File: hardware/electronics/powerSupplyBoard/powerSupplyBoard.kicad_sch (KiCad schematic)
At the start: 27 parts, among them J1 USB_C_Receptacle_USB2.0, J3 615004143821, J4 PRPC009SBAN-M71RC, SW1 PTS647, SW2 SS-12D07, U1 STM32L052K6, U2 AP2112K-3.3, U3 SN65HVD230QDR, Y1 ECS-327ATQMV

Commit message: fixed properties for Tag-Connect and push button
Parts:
- J2: DKPN (none) -> N/A; MPN (none) -> N/A; Manufacturer (none) -> N/A
- SW1: DKPN (none) -> PTS647SK38SMTR2LFSCT-ND; MPN (none) -> PTS 647 SK38 SMTR2 LFS; Manufacturer (none) -> C&K
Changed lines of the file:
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@@
 			)
 		)
-		(property "Datasheet" "~"
+		(property "Datasheet" "datasheets/CK-Switches-PTS647.pdf"
 			(at 196.85 110.49 0)
 			(effects
@@
 			)
 		)
-		(property "Manufacturer" "~"
+		(property "Manufacturer" "C&K"
 			(at 196.85 111.125 0)
 			(do_not_autoplace yes)
@@
 			)
 		)
-		(property "MPN" "~"
+		(property "MPN" "PTS 647 SK38 SMTR2 LFS"
 			(at 196.85 110.49 0)
 			(effects
@@
 			)
 		)
-		(property "DKPN" "~"
+		(property "DKPN" "PTS647SK38SMTR2LFSCT-ND"
 			(at 196.85 110.49 0)
 			(effects
@@
 			)
 		)
-		(property "Description" ""
+		(property "Description" "Tag-Connect TC2050-FP board connector"
 			(at 87.63 135.89 0)
 			(effects
@@
 			)
 		)
-		(property "Manufacturer" "~"
+		(property "Manufacturer" "N/A"
 			(at 87.63 135.89 0)
 			(effects
@@
 			)
 		)
-		(property "MPN" "~"
+		(property "MPN" "N/A"
 			(at 87.63 135.89 0)
 			(effects
@@
 			)
 		)
-		(property "DKPN" "~"
+		(property "DKPN" "N/A"
 			(at 87.63 135.89 0)
 			(effects

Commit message: redefined footprint paths
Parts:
- C1, C2: footprint DS-Capacitors-SMD:MLCC0805 -> lib_fp:MLCC0805
- C10, C11, C5: footprint DS-Capacitors-SMD:MLCC0603 -> lib_fp:MLCC0603; MPN 06035C104K4T4A -> KAM15AR71H104KM
- C3: footprint DS-Capacitors-SMD:MLCC0603 -> lib_fp:MLCC0603; MPN 0805ZC475MAT2A -> KGM21AR71A475MU
- C4, C7, C8, C9: footprint DS-Capacitors-SMD:MLCC0603 -> lib_fp:MLCC0603
- C6: footprint DS-Capacitors-SMD:MLCC0805 -> lib_fp:MLCC0603
- J1: footprint DS-Connector-USB:MOLEX_2171790001 -> lib_fp:MOLEX_2171790001
- J2: footprint DS-Connectors-SMD:TC2050-FP -> lib_fp:TC2050-FP
- J3: footprint DS-Connectors-Network:615004143821 -> lib_fp:615004143821
- J4: footprint DS-Rectangular-Connectors:conn_01x09_254_right_angle -> lib_fp:conn_01x09_254_right_angle
- R1, R2, R3, R4, R5, R6: footprint DS-Resistors-SMD:CRCW0603 -> lib_fp:CRCW0603
- SW1: footprint DS-Switches:SW_4.5x4.5 -> lib_fp:SW_4.5x4.5
- SW2: footprint DS-Switches:SS-12D07-VG_GA_PA -> lib_fp:SS-12D07-VG_GA_PA
- U1: footprint DS-Microcontrollers:UFQFPN32 -> lib_fp:UFQFPN32
- U2: footprint DS-Package-SO:SOT23-5P95_280X300X110L40X38N -> lib_fp:SOT23-5P95_280X300X110L40X38N
- U3: footprint DS-Package-SO:SOIC8P127_490X600X195L83X42N -> lib_fp:SOIC8P127_490X600X195L83X42N
- Y1: footprint DS-Crystals:EXC-34Q -> lib_fp:EXC-34Q
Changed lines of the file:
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@@
 			)
 		)
-		(property "Footprint" "DS-Capacitors-SMD:MLCC0603"
+		(property "Footprint" "lib_fp:MLCC0603"
 			(at 114.3 51.435 0)
 			(effects
@@
 			)
 		)
-		(property "MPN" "06035C104K4T4A"
+		(property "MPN" "KAM15AR71H104KM"
 			(at 114.3 51.435 0)
 			(effects
@@
 			)
 		)
-		(property "Footprint" "DS-Switches:SW_4.5x4.5"
+		(property "Footprint" "lib_fp:SW_4.5x4.5"
 			(at 207.645 110.49 0)
 			(effects
@@
 			)
 		)
-		(property "Footprint" "DS-Capacitors-SMD:MLCC0603"
+		(property "Footprint" "lib_fp:MLCC0603"
 			(at 99.06 51.435 0)
 			(effects
@@
 			)
 		)
-		(property "MPN" "0805ZC475MAT2A"
+		(property "MPN" "KGM21AR71A475MU"
 			(at 99.06 51.435 0)
 			(effects
@@
 			)
 		)
-		(property "Footprint" "DS-Connector-USB:MOLEX_2171790001"
+		(property "Footprint" "lib_fp:MOLEX_2171790001"
 			(at 25.4 38.1 0)
 			(effects
@@
 			)
 		)
-		(property "Footprint" "DS-Microcontrollers:UFQFPN32"
+		(property "Footprint" "lib_fp:UFQFPN32"
 			(at 104.14 88.9 0)
 			(effects
@@
 			)
 		)
-		(property "Footprint" "DS-Package-SO:SOT23-5P95_280X300X110L40X38N"
+		(property "Footprint" "lib_fp:SOT23-5P95_280X300X110L40X38N"
 			(at 72.39 19.05 0)
 			(effects
@@
 			)
 		)
-		(property "Footprint" "DS-Capacitors-SMD:MLCC0603"
+		(property "Footprint" "lib_fp:MLCC0603"
 			(at 184.15 109.855 0)
 			(effects
@@
 			)
 		)
-		(property "Footprint" "DS-Resistors-SMD:CRCW0603"
+		(property "Footprint" "lib_fp:CRCW0603"
 			(at 38.1 24.13 0)
 			(effects
@@
 			)
 		)
-		(property "Footprint" "DS-Switches:SS-12D07-VG_GA_PA"
+		(property "Footprint" "lib_fp:SS-12D07-VG_GA_PA"
 			(at 177.8 127 0)
 			(effects
@@
 			)
 		)
-		(property "Footprint" "DS-Package-SO:SOIC8P127_490X600X195L83X42N"
+		(property "Footprint" "lib_fp:SOIC8P127_490X600X195L83X42N"
 			(at 78.74 76.2 0)
 			(effects
@@
 			)
 		)
-		(property "Footprint" "DS-Capacitors-SMD:MLCC0805"
+		(property "Footprint" "lib_fp:MLCC0603"
 			(at 172.72 51.435 0)
 			(effects
@@
 			)
 		)
-		(property "Footprint" "DS-Resistors-SMD:CRCW0603"
+		(property "Footprint" "lib_fp:CRCW0603"
 			(at 177.8 80.01 0)
 			(effects
@@
 			)
 		)
-		(property "Footprint" "DS-Resistors-SMD:CRCW0603"
+		(property "Footprint" "lib_fp:CRCW0603"
 			(at 166.37 127 90)
 			(effects
@@
 			)
 		)
-		(property "Footprint" "DS-Capacitors-SMD:MLCC0805"
+		(property "Footprint" "lib_fp:MLCC0805"
 			(at 82.55 24.765 0)
 			(effects
@@
 			)
 		)
-		(property "Footprint" "DS-Capacitors-SMD:MLCC0603"
+		(property "Footprint" "lib_fp:MLCC0603"
 			(at 179.07 104.775 0)
 			(effects
@@
 			)
 		)
-		(property "Footprint" "DS-Capacitors-SMD:MLCC0603"
+		(property "Footprint" "lib_fp:MLCC0603"
 			(at 88.9 62.865 0)
 			(effects
@@
 			)
 		)
-		(property "MPN" "06035C104K4T4A"
+		(property "MPN" "KAM15AR71H104KM"
 			(at 88.9 62.865 0)
 			(effects
@@
 			)
 		)
-		(property "Footprint" "DS-Resistors-SMD:CRCW0603"
+		(property "Footprint" "lib_fp:CRCW0603"
 			(at 185.42 80.01 0)
 			(effects
@@
 			)
 		)
-		(property "Footprint" "DS-Capacitors-SMD:MLCC0603"
+		(property "Footprint" "lib_fp:MLCC0603"
 			(at 180.34 51.435 0)
 			(effects
@@
 			)
 		)
-		(property "Footprint" "DS-Rectangular-Connectors:conn_01x09_254_right_angle"
+		(property "Footprint" "lib_fp:conn_01x09_254_right_angle"
 			(at 22.86 172.72 0)
 			(effects
@@
 			)
 		)
-		(property "Footprint" "DS-Capacitors-SMD:MLCC0805"
+		(property "Footprint" "lib_fp:MLCC0805"
 			(at 55.88 24.765 0)
 			(effects
@@
 			)
 		)
-		(property "Footprint" "DS-Capacitors-SMD:MLCC0603"
+		(property "Footprint" "lib_fp:MLCC0603"
 			(at 196.85 121.285 0)
 			(effects
@@
 			)
 		)
-		(property "MPN" "06035C104K4T4A"
+		(property "MPN" "KAM15AR71H104KM"
 			(at 196.85 121.285 0)
 			(effects
@@
 			)
 		)
-		(property "Footprint" "DS-Resistors-SMD:CRCW0603"
+		(property "Footprint" "lib_fp:CRCW0603"
 			(at 46.99 24.13 0)
 			(effects
@@
 			)
 		)
-		(property "Footprint" "DS-Resistors-SMD:CRCW0603"
+		(property "Footprint" "lib_fp:CRCW0603"
 			(at 68.58 73.66 0)
 			(effects
@@
 			)
 		)
-		(property "Footprint" "DS-Connectors-Network:615004143821"
+		(property "Footprint" "lib_fp:615004143821"
 			(at 50.8 73.66 0)
 			(effects
@@
 			)
 		)
-		(property "Footprint" "DS-Connectors-SMD:TC2050-FP"
+		(property "Footprint" "lib_fp:TC2050-FP"
 			(at 87.63 135.89 0)
 			(effects
@@
 			)
 		)
-		(property "Footprint" "DS-Crystals:EXC-34Q"
+		(property "Footprint" "lib_fp:EXC-34Q"
 			(at 165.1 101.6 90)
 			(effects
@@
 			)
 		)
-		(property "Footprint" "DS-Capacitors-SMD:MLCC0603"
+		(property "Footprint" "lib_fp:MLCC0603"
 			(at 106.68 51.435 0)
 			(effects

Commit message: updated component references and sizes
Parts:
- removed C11: 100nF, lib_fp:MLCC0603, symbol lib_sch:C_2
- removed J3: 615004143821, lib_fp:615004143821, symbol lib_sch:RJ11
- removed R6: 120R, lib_fp:CRCW0603, symbol lib_sch:R
- removed U3: SN65HVD230QDR, lib_fp:SOIC8P127_490X600X195L83X42N, symbol lib_sch:SN65HVD23xQ
- C1, C2: DKPN 478-KGM21AR71C106KUCT-ND -> 478-KAM21AR71A106MUCT-ND; MPN KGM21AR71C106KU -> KAM21AR71A106MU; Tolerance 10% -> 20%; Voltage Rating 16V -> 10V
- C3: DKPN 478-KGM21AR71A475MUCT-ND -> 478-KAM15CR70J475KTCT-ND; MPN KGM21AR71A475MU -> KAM15CR70J475KT; Package 0805 -> 0603; Tolerance 20% -> 10%; Voltage Rating 10V -> 6V3
- C6: DKPN 478-KGM21AR71H105KLCT-ND -> 478-KAM15AR71C105KTCT-ND; MPN 08055C105KAT4A -> KAM15AR71C105KT; Package 0805 -> 0603; Voltage Rating 50V -> 16V
- C7: footprint lib_fp:MLCC0603 -> lib_fp:MLCC0402; DKPN 478-KGM15AR71C103KTCT-ND -> 478-KAM05AR71H103KHCT-ND; MPN KGM15AR71C103KT -> KAM05AR71H103KH; Package 0603 -> 0402; Voltage Rating 16V -> 50V
- R1, R2: footprint lib_fp:CRCW0603 -> lib_fp:CRCW0402; DKPN 541-5.1KGCT-ND -> 541-5.10KLCT-ND; MPN CRCW06035K10JNEA -> CRCW04025K10FKED; Package 0603 -> 0402; Power Rating 100mW -> 62.5mW; Tolerance 5% -> 1%
- R3, R4, R5: footprint lib_fp:CRCW0603 -> lib_fp:CRCW0402; DKPN 541-10KGCT-ND -> 541-10KJCT-ND; MPN CRCW060310K0JNEA -> CRCW040210K0JNED; Package 0603 -> 0402; Power Rating 100mW -> 62.5mW
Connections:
- net CAN_MODE: no longer names the net of U1.10 (PA4)
- net CAN_RXD: no longer names the net of U1.9 (PA3)
- net CAN_TXD: no longer names the net of U1.8 (PA2)
- no-connect marks 14 -> 15
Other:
- note removed: "+3V3 CANbus Transceiver"
- note removed: "RJ11 Jack"
- moved on the sheet: J4

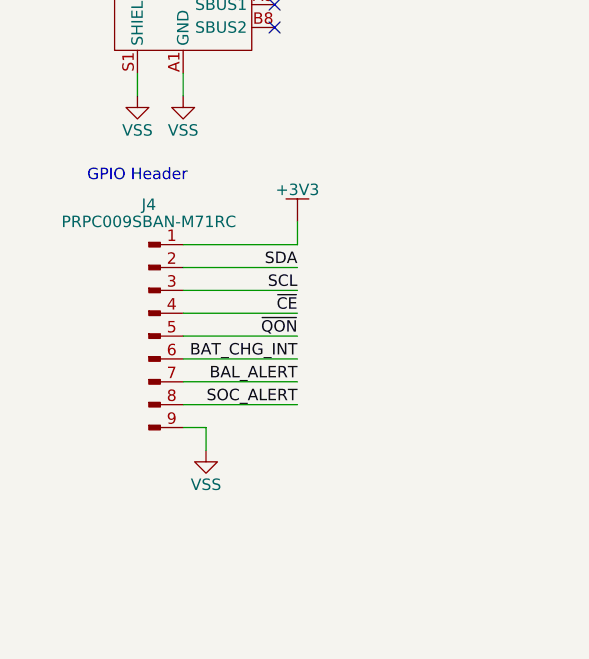
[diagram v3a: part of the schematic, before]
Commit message: removed gpio header
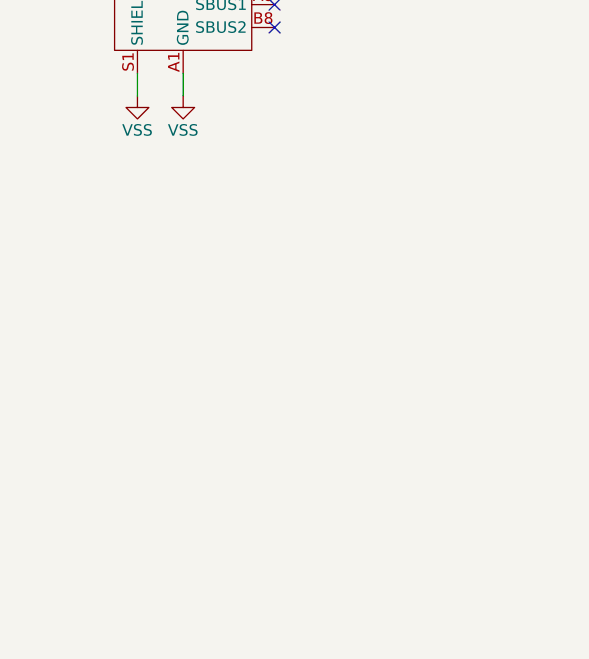
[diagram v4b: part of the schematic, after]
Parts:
- removed J4: PRPC009SBAN-M71RC, lib_fp:conn_01x09_254_right_angle, symbol lib_sch:Conn_01x09_Pin
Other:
- note removed: "GPIO Header"

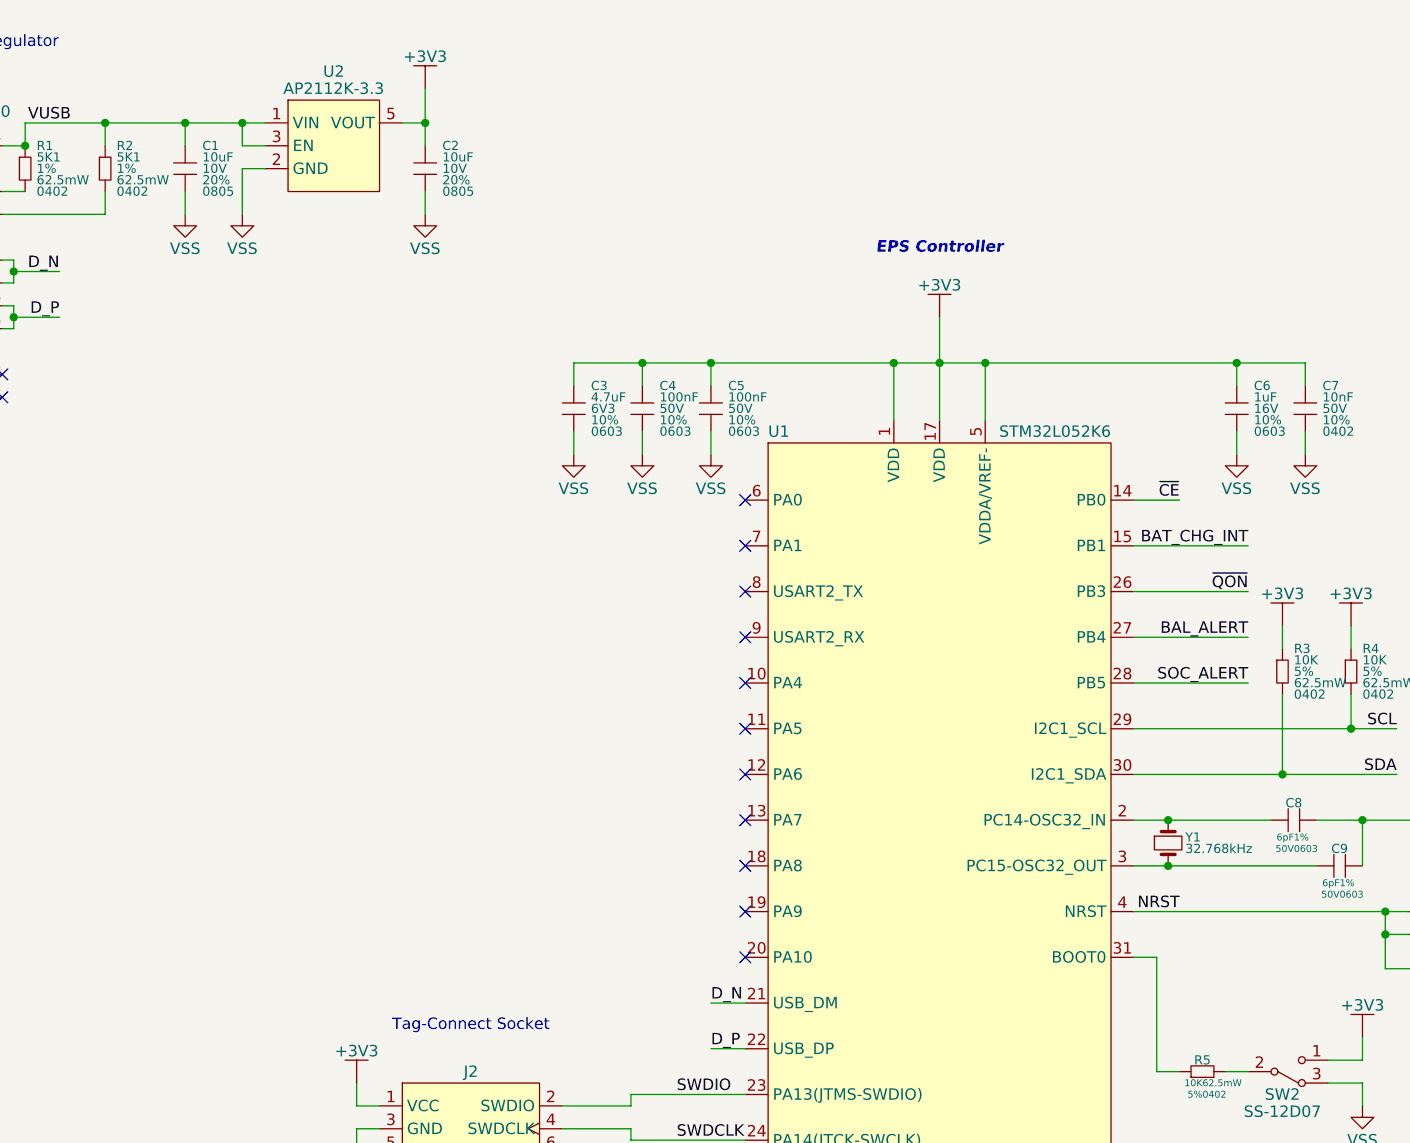
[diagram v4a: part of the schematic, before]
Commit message: added LEDs and remapped some pins for easier routing
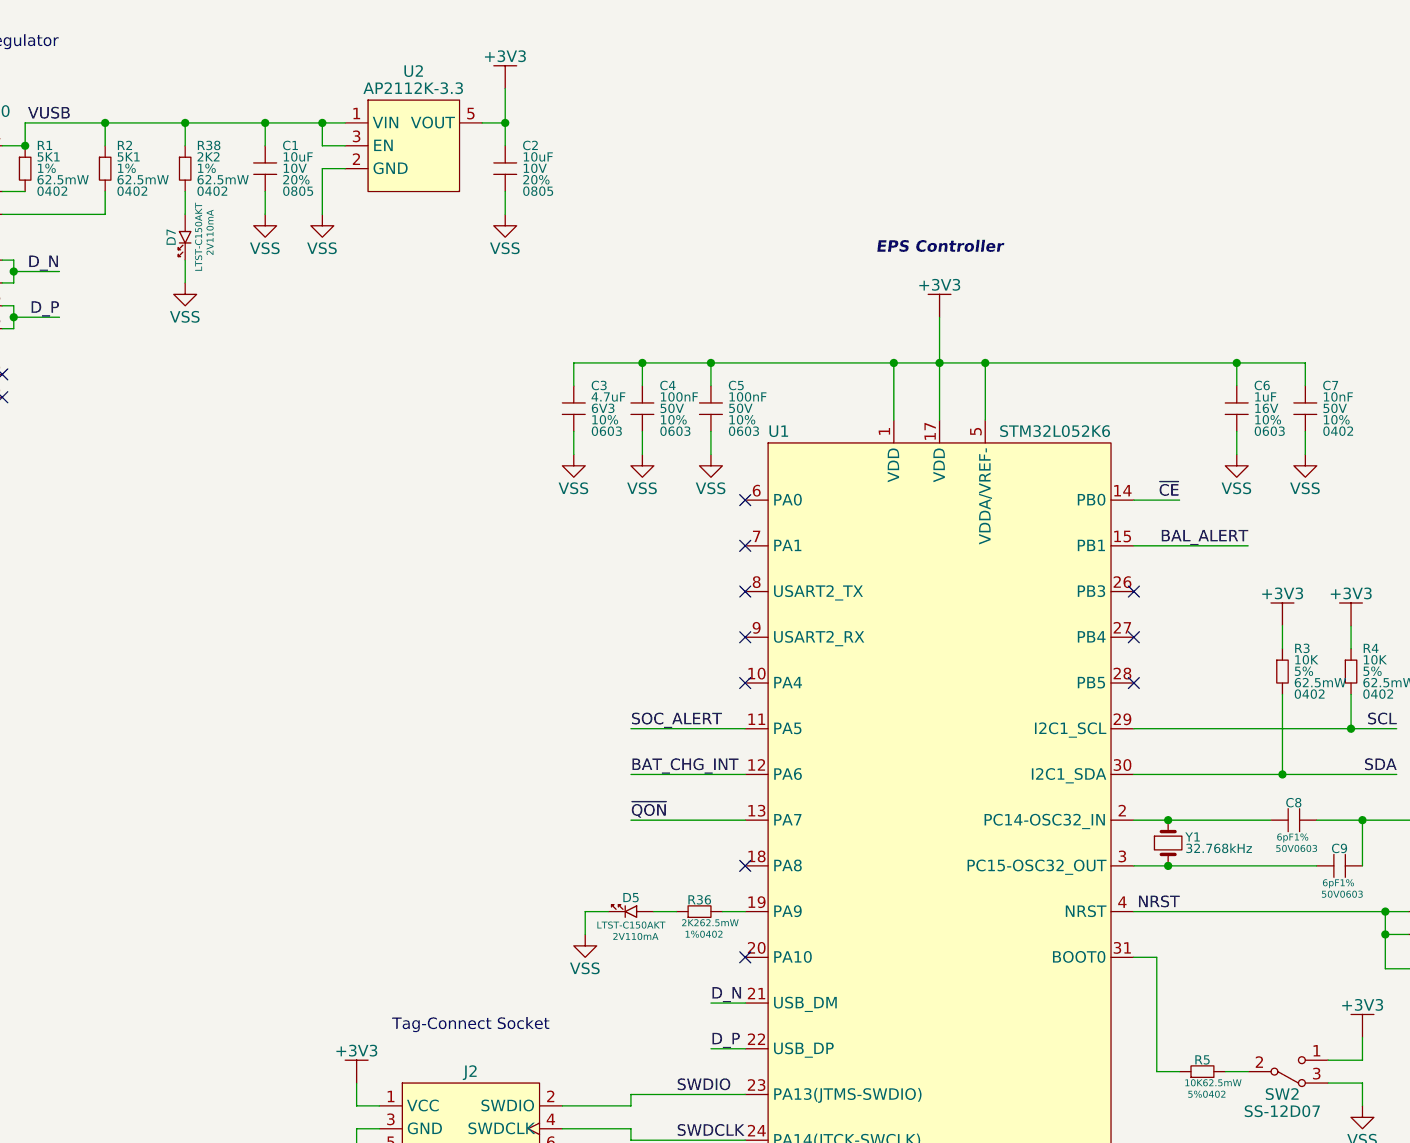
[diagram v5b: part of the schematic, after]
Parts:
- added D5, D7: LTST-C150AKT, lib_fp:LTST-1206, symbol lib_sch:LED_horizontal
- added R36: 2K2, lib_fp:CRCW0402, symbol lib_sch:R_horizontal
- added R38: 2K2, lib_fp:CRCW0402, symbol lib_sch:R
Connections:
- net BAL_ALERT: now also U1.15 (PB1); no longer U1.27 (PB4)
- net BAT_CHG_INT: now also U1.12 (PA6); no longer U1.15 (PB1)
- net SOC_ALERT: now also U1.11 (PA5); no longer U1.28 (PB5)
- net VSS: now also D5.2, D7.2
- net VUSB: now also R38.1
- net ~{QON}: now also U1.13 (PA7); no longer U1.26 (PB3)
- net at U1.19 (PA9): now also R36.2
- new net: D7.1, R38.2
- new net: D5.1, R36.1
- no-connect marks 15 -> 14
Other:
- moved on the sheet: C1, C2, U2
